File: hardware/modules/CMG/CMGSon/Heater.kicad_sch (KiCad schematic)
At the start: 36 parts, among them J1 THR1, J2 THR2, J3 THR3, J5 Heater, J6 HeaterLiPo, Q1 NMOS, U1 MCP3424x-xSL, U13 INA226, U2 MCP1501-20xCH

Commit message: 一旦回路図完成
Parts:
- removed R1: 10k, Resistor_SMD:R_0402_1005Metric, symbol Device:R
- added R302: 10k, Resistor_SMD:R_0402_1005Metric, symbol Device:R
- renumbered C15 to C301, C16 to C302, C801 to C303, C802 to C304, C3 to C305, C4 to C306, C5 to C307, C1 to C308, C2 to C309, C22 to C310, C19 to C311, C17 to C312, F302 to F301, J6 to J301, J1 to J302, J2 to J303, J5 to J304, J3 to J305, LED103 to LED301, Q1 to Q301, R2 to R301, R102 to R303, R3 to R304, R4 to R305, R107 to R306, R104 to R307, R5 to R308, R6 to R309, R108 to R310, R25 to R311, R23 to R312, R24 to R313, U13 to U301, U1 to U302, U2 to U303
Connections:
- net GND: now also R302.2
- net at J302.2 (Pin_2), R301.2: now also R302.1

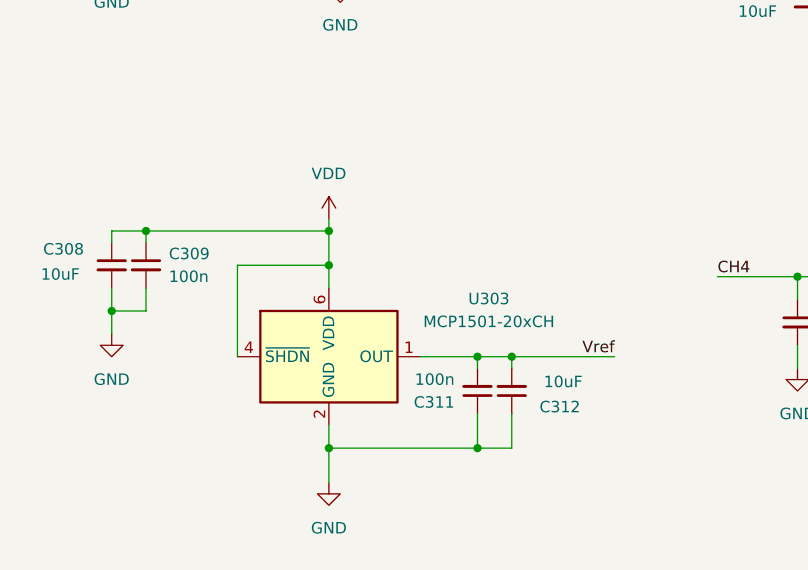
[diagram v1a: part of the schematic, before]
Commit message: フットプリント割り当て完了
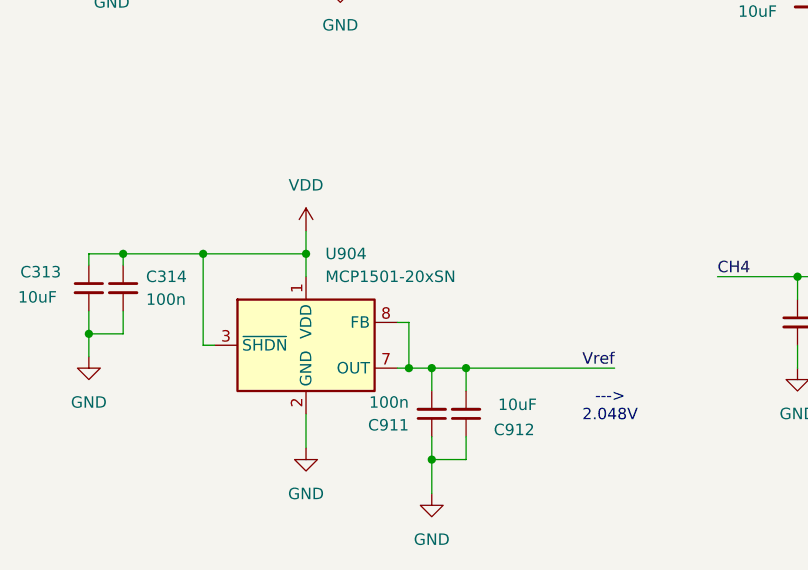
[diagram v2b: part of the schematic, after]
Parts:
- removed C308: 10uF, Capacitor_SMD:C_0603_1608Metric, symbol Device:C_Small
- removed C309: 100n, Capacitor_SMD:C_0402_1005Metric, symbol Device:C_Small
- removed U303: MCP1501-20xCH, Package_TO_SOT_SMD:SOT-23-6, symbol Reference_Voltage:MCP1501-20xCH
- added C313: 10uF, Capacitor_SMD:C_0603_1608Metric, symbol Device:C_Small
- added C314: 100n, Capacitor_SMD:C_0402_1005Metric, symbol Device:C_Small
- added U904: MCP1501-20xSN, Package_SO:SOIC-8_3.9x4.9mm_P1.27mm, symbol Reference_Voltage:MCP1501-20xSN
- Q301: footprint (none) -> Package_TO_SOT_SMD:SOT-23-3; LCSC (none) -> C20917
- renumbered C311 to C911, C312 to C912
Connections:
- net GND: now also Q301.1 (S), C313.2, C314.2, U904.2 (GND), U904.4 (GND), U904.5 (GND), U904.6 (GND); no longer Q301.3 (S)
- net VDD: now also C313.1, C314.1, U904.1 (VDD), U904.3 (~{SHDN})
- net Vref: now also U904.7 (OUT), U904.8 (FB)
- net at R306.1, R307.1: now also Q301.1 (S); no longer Q301.2 (G)
- net at J304.2 (Pin_2): now also Q301.3 (D); no longer Q301.1 (D)
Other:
- note added: "---> 2.048V"
- moved on the sheet: C911, C912

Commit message: LogicBoard一旦完成
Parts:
- removed R310: 1k, Resistor_SMD:R_0402_1005Metric, symbol Device:R
- added R5: 470, Resistor_SMD:R_0402_1005Metric, symbol Device:R
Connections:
- net GND: now also R5.2
- net at LED301.1 (K): now also R5.1
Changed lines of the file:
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@@
-	(symbol
-		(lib_id "Device:R")
-		(at 212.09 123.19 0)
-		(mirror y)
-		(unit 1)
-		(exclude_from_sim no)
-		(in_bom yes)
-		(on_board yes)
-		(dnp no)
-		(property "Reference" "R310"
-			(at 215.9 121.92 0)
-			(effects
-				(font
-					(size 1.27 1.27)
-				)
-			)
-		)
-		(property "Value" "1k"
-			(at 215.9 124.46 0)
-			(effects
-				(font
-					(size 1.27 1.27)
-				)
-			)
-		)
-		(property "Footprint" "Resistor_SMD:R_0402_1005Metric"
-			(at 213.868 123.19 90)
-			(effects
-				(font
-					(size 1.27 1.27)
-				)
-				(hide yes)
-			)
-		)
-		(property "Datasheet" "~"
-			(at 212.09 123.19 0)
-			(effects
-				(font
-					(size 1.27 1.27)
-				)
-				(hide yes)
-			)
-		)
-		(property "Description" "Resistor"
-			(at 212.09 123.19 0)
-			(effects
-				(font
-					(size 1.27 1.27)
-				)
-				(hide yes)
-			)
-		)
-		(property "LCSC" "C25123"
-			(at 212.09 123.19 0)
-			(effects
-				(font
-					(size 1.27 1.27)
-				)
-				(hide yes)
-			)
-		)
-		(pin "1"
-		)
-		(pin "2"
-		)
-		(instances
-			(project "Heater"
-				(path "/4eb245a9-6c21-4f00-ae42-6a498711dd85/c55431da-8938-47ef-8924-54f36b792cab"
-					(reference "R310")
-					(unit 1)
-				)
-			)
-			(project "Heater"
-				(path "/861a27ed-ba4b-4fa4-8155-a8d1929fc215"
-					(reference "R108")
-					(unit 1)
-				)
-			)
-		)
-	)
 	(symbol
 		(lib_id "Device:R")
@@
 					(unit 1)
 				)
+			)
+		)
+	)
+	(symbol
+		(lib_id "Device:R")
+		(at 212.09 123.19 0)
+		(unit 1)
+		(exclude_from_sim no)
+		(in_bom yes)
+		(on_board yes)
+		(dnp no)
+		(fields_autoplaced yes)
+		(property "Reference" "R5"
+			(at 214.63 121.92 0)
+			(effects
+				(font
+					(size 1.27 1.27)
+				)
+				(justify left)
+			)
+		)
+		(property "Value" "470"
+			(at 214.63 124.46 0)
+			(effects
+				(font
+					(size 1.27 1.27)
+				)
+				(justify left)
+			)
+		)
+		(property "Footprint" "Resistor_SMD:R_0402_1005Metric"
+			(at 210.312 123.19 90)
+			(effects
+				(font
+					(size 1.27 1.27)
+				)
+				(hide yes)
+			)
+		)
+		(property "Datasheet" "~"
+			(at 212.09 123.19 0)
+			(effects
+				(font
+					(size 1.27 1.27)
+				)
+				(hide yes)
+			)
+		)
+		(property "Description" ""
+			(at 212.09 123.19 0)
+			(effects
+				(font
+					(size 1.27 1.27)
+				)
+				(hide yes)
+			)
+		)
+		(property "LCSC" "C25117"
+			(at 212.09 123.19 0)
+			(effects
+				(font
+					(size 1.27 1.27)
+				)
+				(hide yes)
+			)
+		)
+		(pin "1"
+		)
+		(pin "2"
+		)
+		(instances
+			(project "CMGSon"
+				(path "/4eb245a9-6c21-4f00-ae42-6a498711dd85/c55431da-8938-47ef-8924-54f36b792cab"
+					(reference "R5")
+					(unit 1)
+				)

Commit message: 途中
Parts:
- J302, J303, J305: footprint Connector_JST:JST_PH_S2B-PH-K_1x02_P2.00mm_Horizontal -> Connector_JST:JST_PH_B2B-PH-K_1x02_P2.00mm_Vertical
- renumbered C313 to C308, C314 to C309, C911 to C311, C912 to C312, R5 to R310, U904 to U303
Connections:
- net CH2: now also C310.1, R312.1; no longer C306.1, R304.1
- net CH4: now also C306.1, R304.1; no longer C310.1, R312.1
- net GND: now also Q301.2 (S); no longer Q301.1 (S)
- net at R303.1, U301.9 (Vin-): now also J304.2 (Pin_1); no longer J304.1 (Pin_1)
- net at Q301.3 (D): now also J304.1 (Pin_2); no longer J304.2 (Pin_2)
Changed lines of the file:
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@@
 		)
 	)
-	(label "CH4"
-		(at 115.57 153.67 0)
-		(effects
-			(font
-				(size 1.27 1.27)
-			)
-			(justify left bottom)
-		)
-	)
 	(label "Vref"
 		(at 135.89 62.23 0)
@@
 		)
 	)
-	(label "CH2"
+	(label "CH4"
 		(at 116.84 91.44 0)
 		(effects
@@
 		)
 	)
+	(label "CH2"
+		(at 115.57 153.67 0)
+		(effects
+			(font
+				(size 1.27 1.27)
+			)
+			(justify left bottom)
+		)
+	)
 	(label "CH1"
 		(at 116.84 64.77 0)
@@
 		(dnp no)
 		(fields_autoplaced yes)
-		(property "Reference" "#PWR0915"
+		(property "Reference" "#PWR0315"
 			(at 69.85 152.4 0)
 			(effects
@@
 			(project "CMGSon"
 				(path "/4eb245a9-6c21-4f00-ae42-6a498711dd85/c55431da-8938-47ef-8924-54f36b792cab"
-					(reference "#PWR0915")
+					(reference "#PWR0315")
 					(unit 1)
 				)
@@
 		(on_board yes)
 		(dnp no)
-		(property "Reference" "C911"
+		(property "Reference" "C311"
 			(at 81.28 170.1737 0)
 			(effects
@@
 			(project "CMGSon"
 				(path "/4eb245a9-6c21-4f00-ae42-6a498711dd85/c55431da-8938-47ef-8924-54f36b792cab"
-					(reference "C911")
+					(reference "C311")
 					(unit 1)
 				)
@@
 		(on_board yes)
 		(dnp no)
-		(property "Reference" "C313"
+		(property "Reference" "C308"
 			(at 38.1 153.162 0)
 			(effects
@@
 			(project "CMGSon"
 				(path "/4eb245a9-6c21-4f00-ae42-6a498711dd85/c55431da-8938-47ef-8924-54f36b792cab"
-					(reference "C313")
+					(reference "C308")
 					(unit 1)
 				)
@@
 		(dnp no)
 		(fields_autoplaced yes)
-		(property "Reference" "R5"
+		(property "Reference" "R310"
 			(at 214.63 121.92 0)
 			(effects
@@
 			(project "CMGSon"
 				(path "/4eb245a9-6c21-4f00-ae42-6a498711dd85/c55431da-8938-47ef-8924-54f36b792cab"
-					(reference "R5")
+					(reference "R310")
 					(unit 1)
 				)
@@
 		(dnp no)
 		(fields_autoplaced yes)
-		(property "Reference" "#PWR0916"
+		(property "Reference" "#PWR0316"
 			(at 45.72 168.91 0)
 			(effects
@@
 			(project "CMGSon"
 				(path "/4eb245a9-6c21-4f00-ae42-6a498711dd85/c55431da-8938-47ef-8924-54f36b792cab"
-					(reference "#PWR0916")
+					(reference "#PWR0316")
 					(unit 1)
 				)
@@
 			)
 		)
-		(property "Footprint" "Connector_JST:JST_PH_S2B-PH-K_1x02_P2.00mm_Horizontal"
+		(property "Footprint" "Connector_JST:JST_PH_B2B-PH-K_1x02_P2.00mm_Vertical"
 			(at 146.05 62.23 0)
 			(effects
@@
 		(dnp no)
 		(fields_autoplaced yes)
-		(property "Reference" "#PWR0918"
+		(property "Reference" "#PWR0319"
 			(at 69.85 179.07 0)
 			(effects
@@
 			(project "CMGSon"
 				(path "/4eb245a9-6c21-4f00-ae42-6a498711dd85/c55431da-8938-47ef-8924-54f36b792cab"
-					(reference "#PWR0918")
+					(reference "#PWR0319")
 					(unit 1)
 				)
@@
 		(dnp no)
 		(fields_autoplaced yes)
-		(property "Reference" "#PWR0919"
+		(property "Reference" "#PWR0320"
 			(at 83.82 184.15 0)
 			(effects
@@
 			(project "CMGSon"
 				(path "/4eb245a9-6c21-4f00-ae42-6a498711dd85/c55431da-8938-47ef-8924-54f36b792cab"
-					(reference "#PWR0919")
+					(reference "#PWR0320")
 					(unit 1)
 				)
@@
 		(on_board yes)
 		(dnp no)
-		(property "Reference" "C314"
+		(property "Reference" "C309"
 			(at 52.07 153.6763 0)
 			(effects
@@
 			(project "CMGSon"
 				(path "/4eb245a9-6c21-4f00-ae42-6a498711dd85/c55431da-8938-47ef-8924-54f36b792cab"
-					(reference "C314")
+					(reference "C309")
 					(unit 1)
 				)
@@
 			)
 		)
-		(property "Footprint" "Connector_JST:JST_PH_S2B-PH-K_1x02_P2.00mm_Horizontal"
+		(property "Footprint" "Connector_JST:JST_PH_B2B-PH-K_1x02_P2.00mm_Vertical"
 			(at 146.05 115.57 0)
 			(effects
@@
 		(dnp no)
 		(fields_autoplaced yes)
-		(property "Reference" "U904"
+		(property "Reference" "U303"
 			(at 71.9933 151.13 0)
 			(effects
@@
 			(project "CMGSon"
 				(path "/4eb245a9-6c21-4f00-ae42-6a498711dd85/c55431da-8938-47ef-8924-54f36b792cab"
-					(reference "U904")
+					(reference "U303")
 					(unit 1)
 				)
@@
 		(pin "3"
 		)
-		(pin "1"
+		(pin "2"
 		)
 		(pin "1"
@@
 	)
 	(symbol
+		(lib_name "Conn_01x02_1")
 		(lib_id "Connector_Generic:Conn_01x02")
 		(at 248.92 92.71 0)
@@
 		(on_board yes)
 		(dnp no)
-		(property "Reference" "C912"
+		(property "Reference" "C312"
 			(at 95.25 170.688 0)
 			(effects
@@
 			(project "CMGSon"
 				(path "/4eb245a9-6c21-4f00-ae42-6a498711dd85/c55431da-8938-47ef-8924-54f36b792cab"
-					(reference "C912")
+					(reference "C312")
 					(unit 1)
 				)
@@
 			)
 		)
-		(property "Footprint" "Connector_JST:JST_PH_S2B-PH-K_1x02_P2.00mm_Horizontal"
+		(property "Footprint" "Connector_JST:JST_PH_B2B-PH-K_1x02_P2.00mm_Vertical"
 			(at 146.05 88.9 0)
 			(effects
